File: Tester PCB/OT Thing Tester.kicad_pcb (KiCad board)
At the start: 2 copper layers, 202 x 88 mm, 84 parts, among them J1 Conn_01x05, J2 Conn_01x08, J3 Conn_01x05, J4 Conn_01x05, J5 Link, J6 Link, Q1 BSP62, Q2 BSP62, Q3 BC847, Q4 BC847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

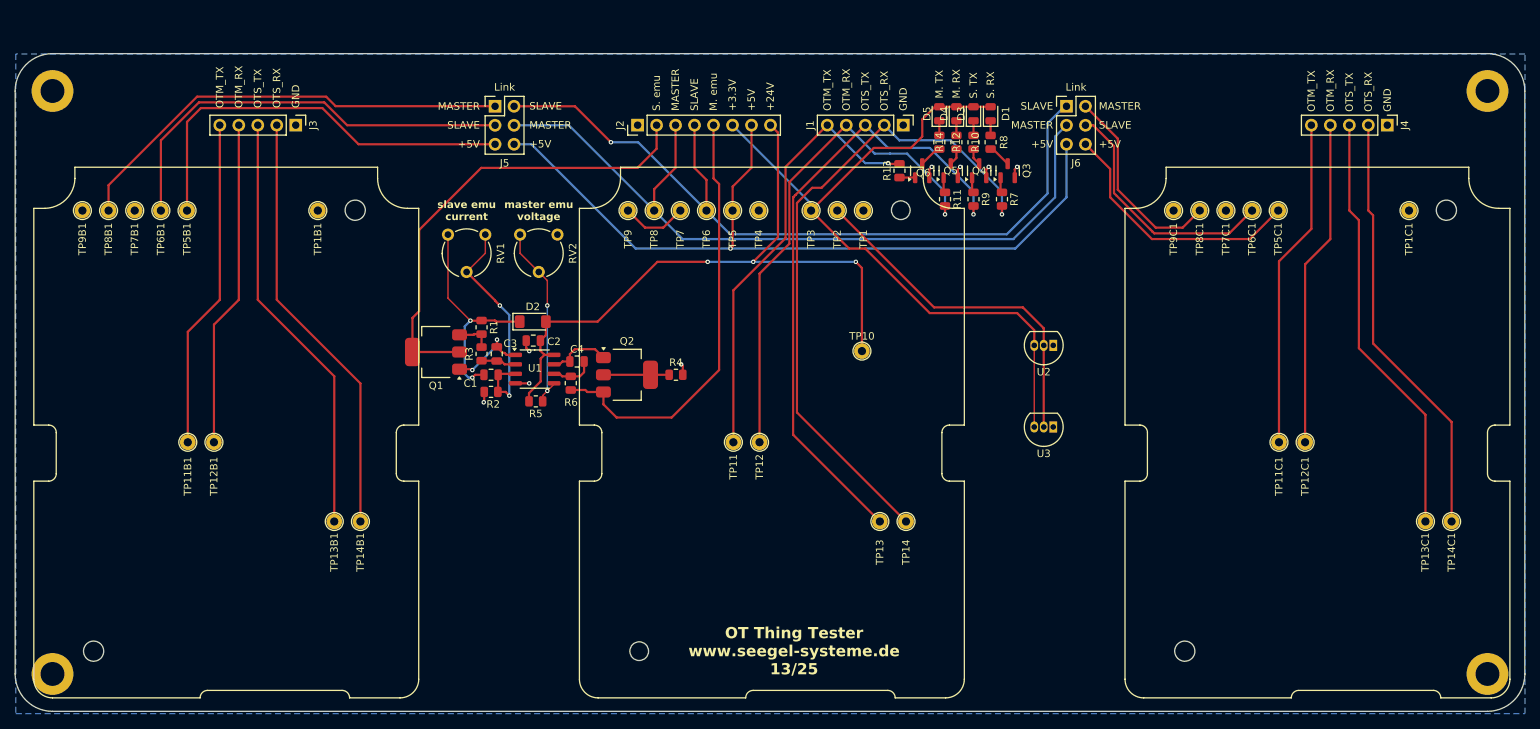
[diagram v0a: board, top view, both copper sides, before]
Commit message: add USB test points single board test w/ power supply
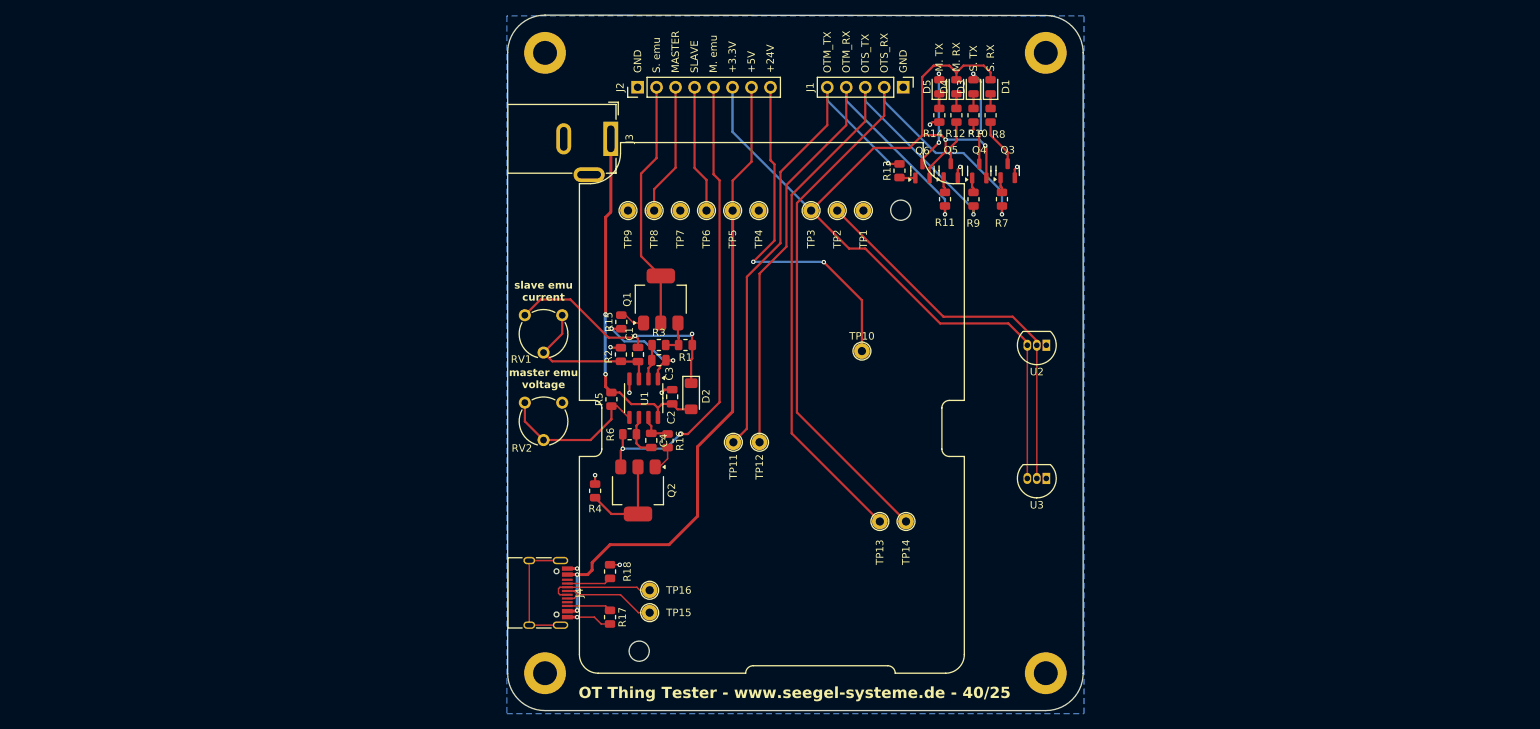
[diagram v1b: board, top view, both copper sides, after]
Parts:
- removed H10, H7, H8, H9: MountingHole, MountingHole:MountingHole_2.7mm_M2.5
- removed J5, J6: Link, Connector_PinHeader_2.54mm:PinHeader_2x03_P2.54mm_Vertical
- removed TP11B1, TP11C1: OTM_TX, Library:TestPoint_THTPad_D2.0mm_Drill1.1mm
- removed TP12B1, TP12C1: OTM_RX, Library:TestPoint_THTPad_D2.0mm_Drill1.1mm
- removed TP13B1, TP13C1: OTS_TX, Library:TestPoint_THTPad_D2.0mm_Drill1.1mm
- removed TP14B1, TP14C1: OTS_RX, Library:TestPoint_THTPad_D2.0mm_Drill1.1mm
- removed TP1B1, TP1C1: GND, Library:TestPoint_THTPad_D2.0mm_Drill1.1mm
- removed TP5B1, TP5C1: 5V, Library:TestPoint_THTPad_D2.0mm_Drill1.1mm
- removed TP6B1, TP6C1: SLAVE+, Library:TestPoint_THTPad_D2.0mm_Drill1.1mm
- removed TP7B1, TP7C1: SLAVE-, Library:TestPoint_THTPad_D2.0mm_Drill1.1mm
- removed TP8B1, TP8C1: MASTER+, Library:TestPoint_THTPad_D2.0mm_Drill1.1mm
- removed TP9B1, TP9C1: MASTER-, Library:TestPoint_THTPad_D2.0mm_Drill1.1mm
- added R15: 4k7, Resistor_SMD:R_0805_2012Metric, F.Cu at (118.6, 97.2)
- added R16: 4k7, Resistor_SMD:R_0805_2012Metric, F.Cu at (124.8, 113.1)
- added R17: 5k1, Resistor_SMD:R_0805_2012Metric, F.Cu at (117.1, 136.7)
- added R18: 5k1, Resistor_SMD:R_0805_2012Metric, F.Cu at (117.1, 130.6)
- added TP15: USB_DP, Library:TestPoint_THTPad_D2.0mm_Drill1.1mm, F.Cu at (122.4, 136.1)
- added TP16: USB_DM, Library:TestPoint_THTPad_D2.0mm_Drill1.1mm, F.Cu at (122.4, 133.1)
- H1, H2: footprint MountingHole:MountingHole_2.5mm -> MountingHole:MountingHole_2.7mm_M2.5
- J3: value Conn_01x05 -> Barrel_Jack_Switch; footprint Connector_PinHeader_2.54mm:PinHeader_1x05_P2.54mm_Vertical -> Connector_BarrelJack:BarrelJack_GCT_DCJ200-10-A_Horizontal
- J4: value Conn_01x05 -> USB_C_Receptacle_USB2.0; footprint Connector_PinHeader_2.54mm:PinHeader_1x05_P2.54mm_Vertical -> Connector_USB:USB_C_Receptacle_HRO_TYPE-C-31-M-12
- Q4, Q6: value BC847 -> BC857
- moved J4 129.8 mm to (107.3, 133.4)
- moved H3 66.1 mm to (108.4, 61.2)
- moved H5 65.9 mm to (108.4, 144.2)
- moved H4 59.3 mm to (175.4, 61.2)
- moved H6 59.1 mm to (175.4, 144.2)
- moved J3 42.2 mm to (117.2, 72.7)
- moved Q1 30.9 mm to (123.9, 94.2), turned to 90 degrees
- moved R1 27.4 mm to (127.2, 100.3), turned to 180 degrees
- moved R3 23.8 mm to (123.6, 100.3), turned to 0 degrees
- moved D2 23.4 mm to (128.0, 107.1), turned to -90 degrees
- moved RV2 22.5 mm to (105.7, 108.0)
- moved C3 21.7 mm to (123.6, 102.3), turned to 0 degrees
- moved C2 20.0 mm to (125.4, 107.2), turned to 90 degrees
- moved C1 19.8 mm to (120.8, 101.6), turned to 90 degrees
- moved R4 18.9 mm to (115.1, 119.8), turned to 90 degrees
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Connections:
- C2 pad 1: +24V -> +28V
- C3 pad 2: Net-(Q1-B) -> Net-(C3-Pad2)
- C4 pad 2: Net-(Q2-B) -> Net-(C4-Pad2)
- D2 pad 2: +24V -> +28V
- D3 pad 2: +3.3V -> Net-(D3-A)
- D5 pad 2: +3.3V -> Net-(D5-A)
- J3 pad 1: GND -> +28V
- J3 pad 2: Net-(J3-Pin_2) -> GND
- J3 pad 3: Net-(J3-Pin_3) -> unconnected-(J3-Pad3)
- Q4 pad 2: GND -> +3.3V
- Q4 pad 3: Net-(Q4-C) -> Net-(D3-A)
- Q6 pad 2: GND -> +3.3V
- Q6 pad 3: Net-(Q6-C) -> Net-(D5-A)
- R10 pad 1: Net-(Q4-C) -> GND
- R14 pad 1: Net-(Q6-C) -> GND
- R5 pad 2: +24V -> +28V
- U1 pad 1: Net-(Q1-B) -> Net-(C3-Pad2)
- U1 pad 7: Net-(Q2-B) -> Net-(C4-Pad2)
- U1 pad 8: +24V -> +28V
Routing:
- net /SLAVE+: track 105.7 -> 17.2 mm, vias 1 -> 0
- net /MASTER+: track 103.9 -> 17.7 mm
- net Net-(J5-Pin_1): track 60.6 -> 0.00 mm
- net Net-(J3-Pin_2): track 57.7 -> 0.00 mm
- net Net-(J4-Pin_2): track 57.7 -> 0.00 mm
- net Net-(J5-Pin_3): track 57.5 -> 0.00 mm
- net Net-(J3-Pin_3): track 57.3 -> 0.00 mm
- net Net-(J4-Pin_3): track 57.2 -> 0.00 mm
- net Net-(J5-Pin_5): track 55.9 -> 0.00 mm
- net +28V: track 0.00 -> 47.9 mm, vias 0 -> 2
- net Net-(J4-Pin_5): track 44.2 -> 0.00 mm
- net Net-(J3-Pin_5): track 44.2 -> 0.00 mm
- net Net-(J4-Pin_4): track 43.8 -> 0.00 mm
- net Net-(J3-Pin_4): track 43.8 -> 0.00 mm
- net +24V: track 90.5 -> 48.2 mm, vias 3 -> 2
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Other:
- board size 202 x 88 mm -> 77 x 93 mm
- board text added: "OT Thing Tester - www.seegel-systeme.de - 40/25"
- board text removed: "Link"
- board text removed: "OT Thing Tester www.seegel-systeme.de 13/25"
